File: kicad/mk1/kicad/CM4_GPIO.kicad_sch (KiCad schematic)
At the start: 14 parts, among them J22 ARJM11, U19 74LVC1G07SE-7, U20 TPD4EUSB30, U21 TPD4EUSB30

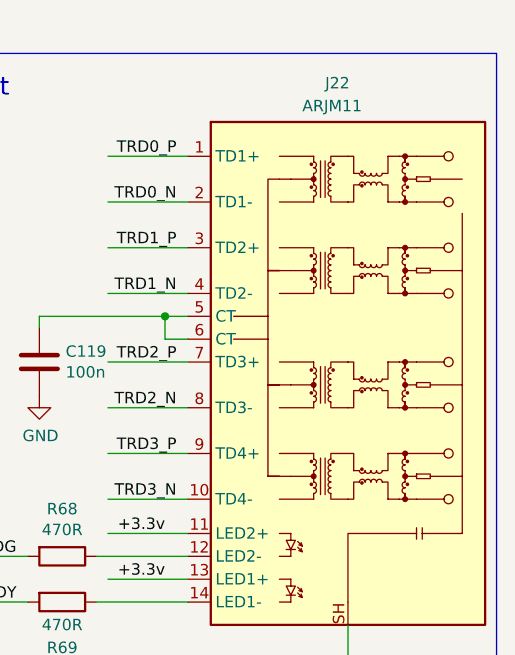
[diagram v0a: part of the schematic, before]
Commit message: work on schematics
* add power rail
* import CM4 related part
* design most of the BMC-PHY part
* create new library/footprint for rp t113-s3 SOM
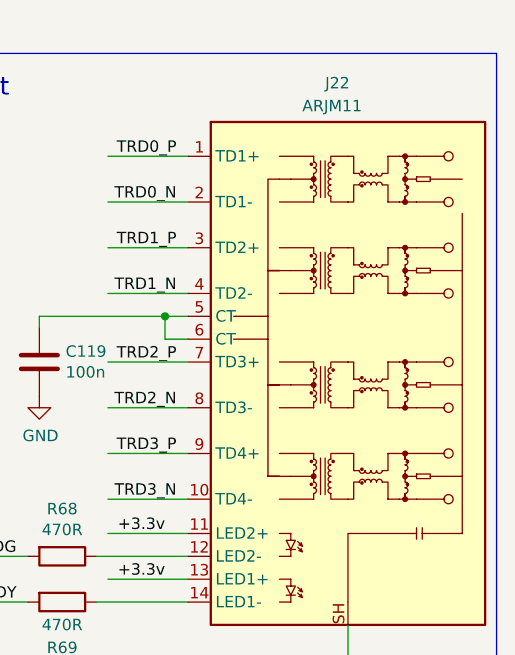
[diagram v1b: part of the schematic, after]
